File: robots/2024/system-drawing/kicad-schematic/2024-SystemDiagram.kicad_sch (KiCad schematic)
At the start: 184 parts

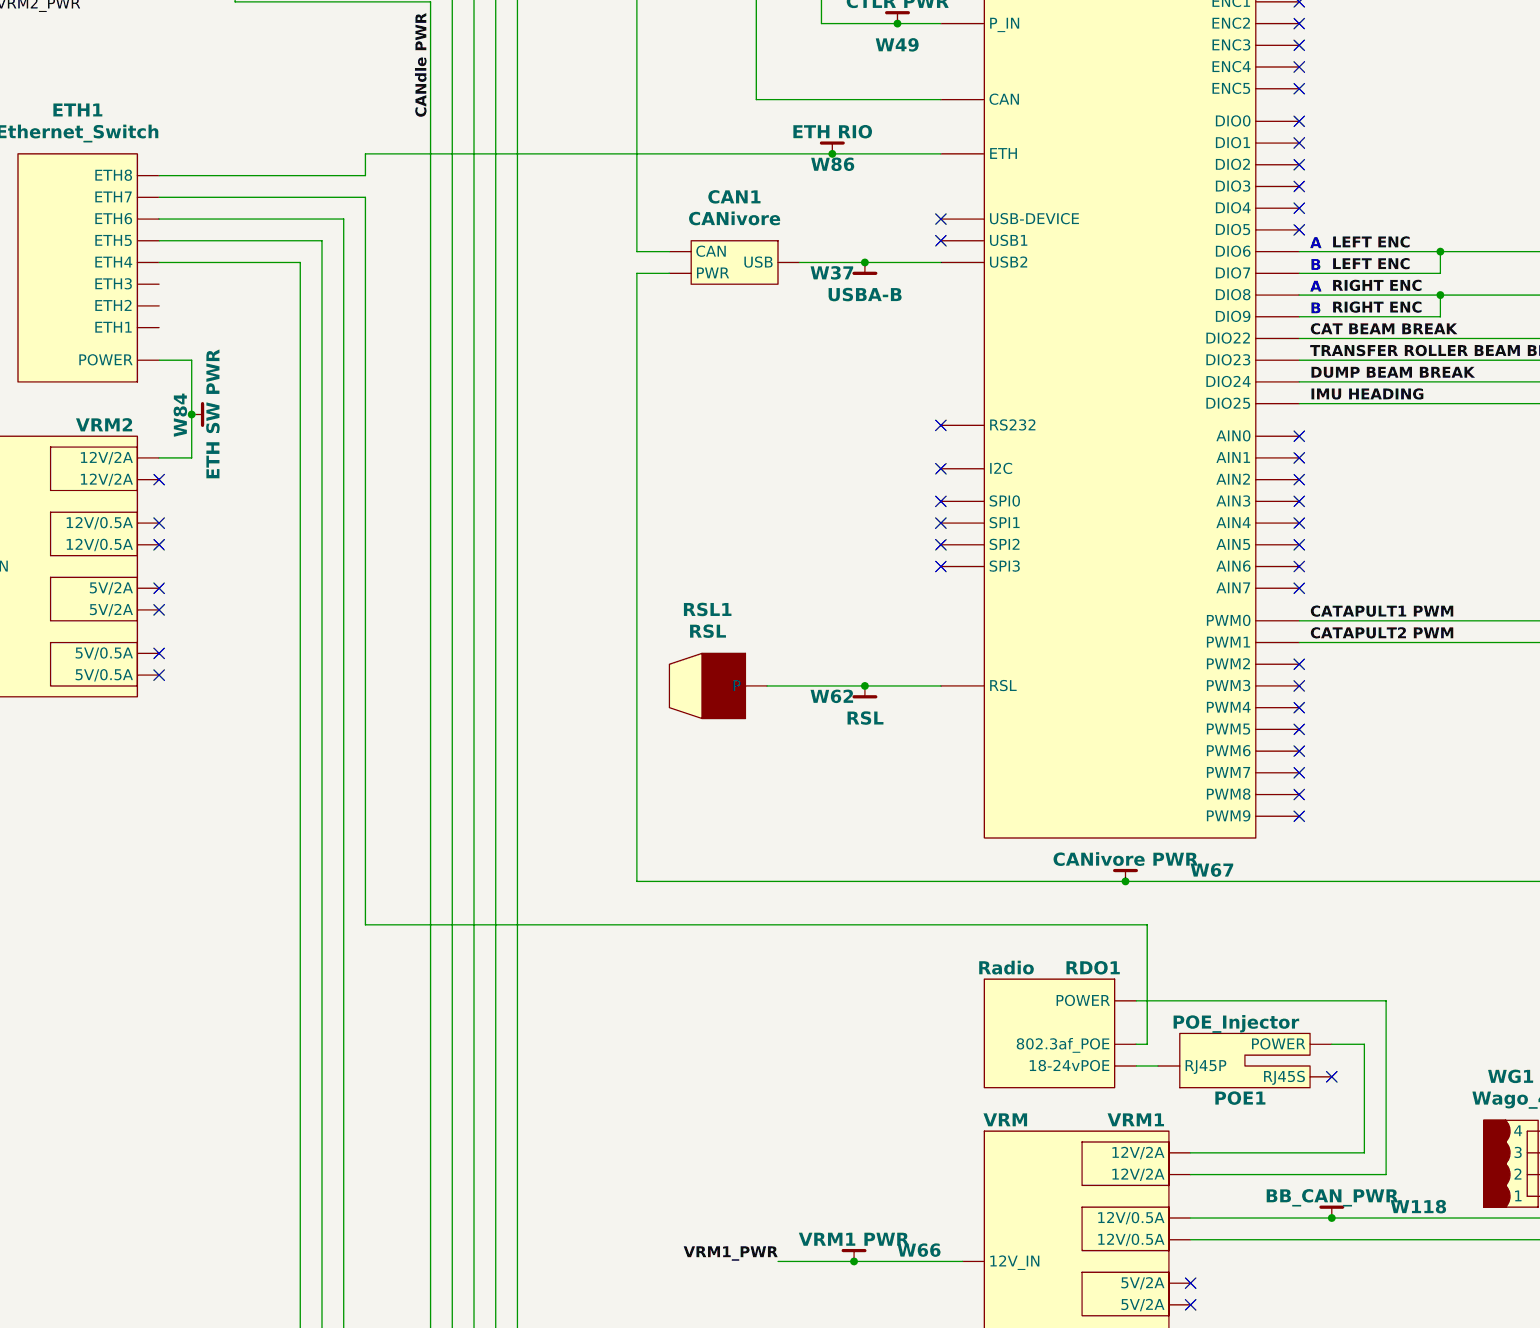
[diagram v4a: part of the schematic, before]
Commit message: Modified sys dwg rio ethernet, added comment to nx adapter
Signed-off-by: Scott Berman <sgberman1@gmail.com>
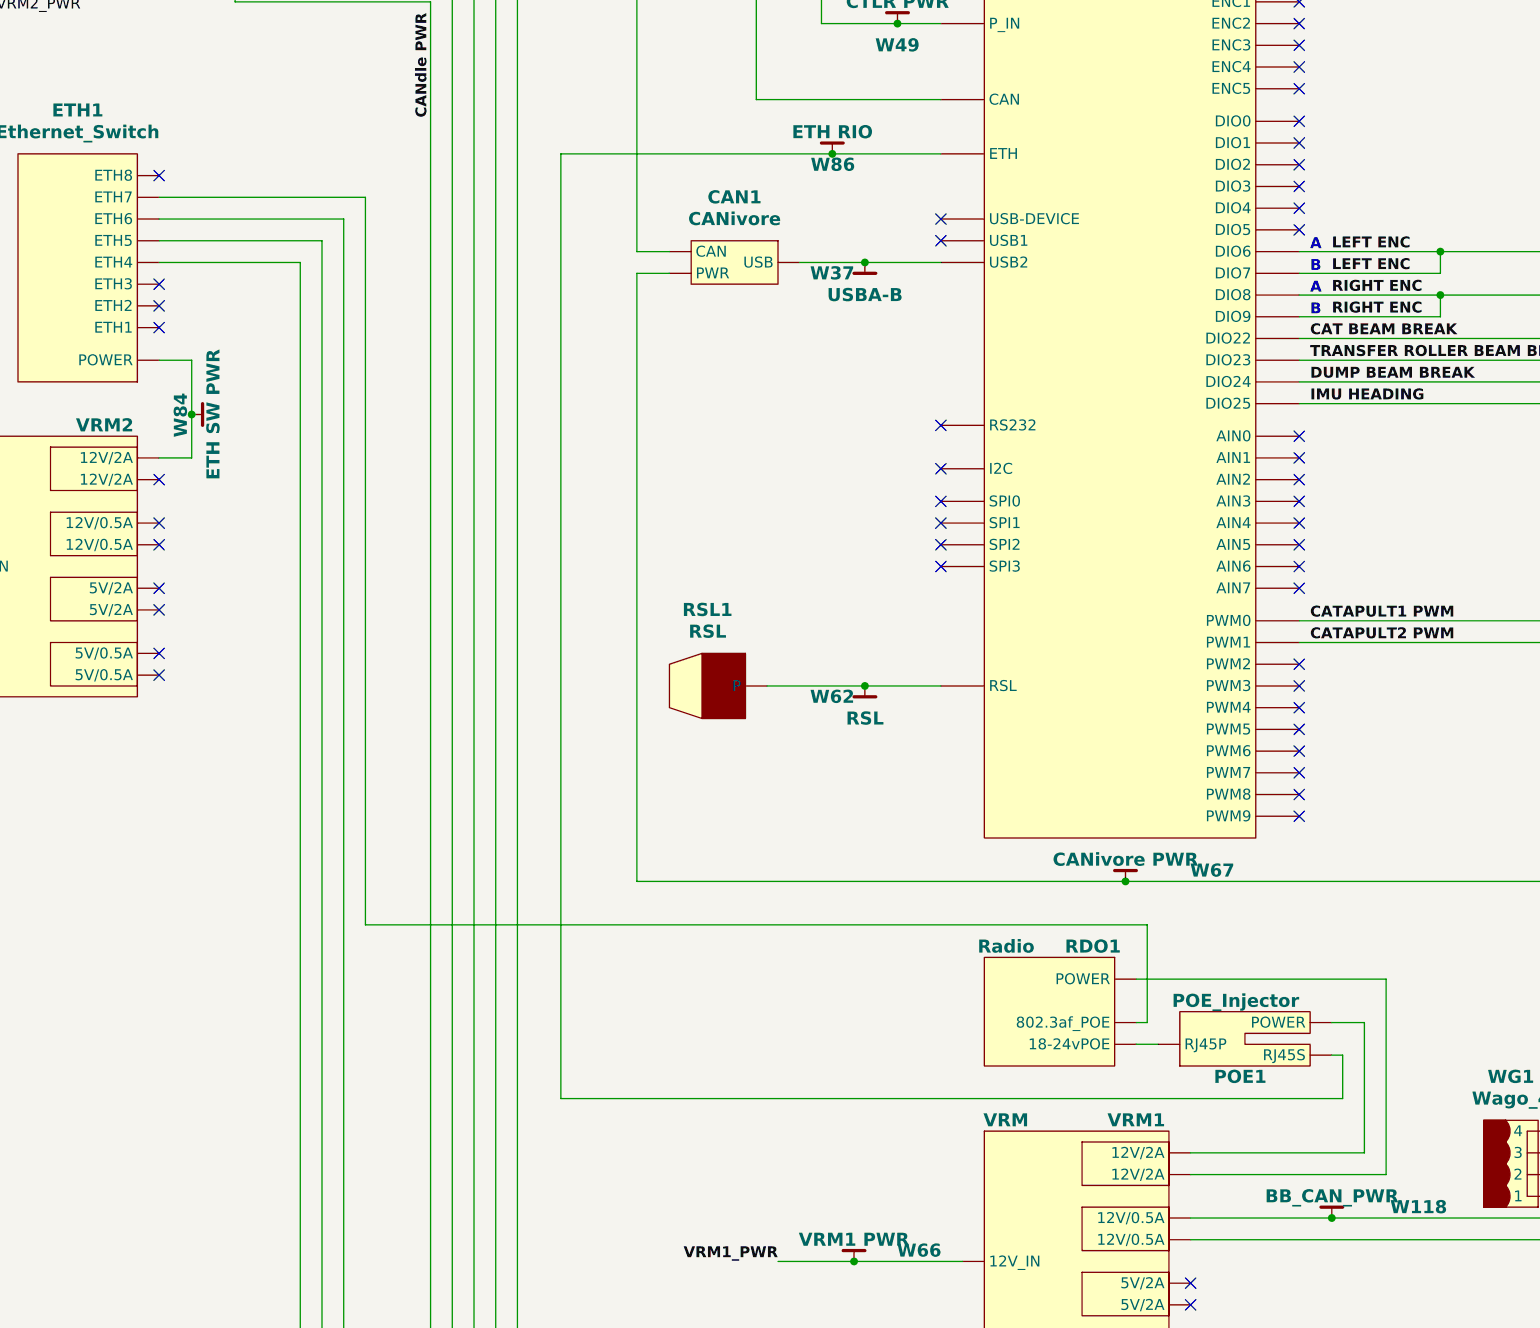
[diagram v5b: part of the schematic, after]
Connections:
- net at POE1. (RJ45S): now also RDO1. (POWER); no longer VRM1. (5V/2A)
- net at RDO1. (POWER): now also ETH1. (POWER); no longer VRM1. (5V/2A)
- net at RIO1.ETH, W86.: now also POE1. (RJ45S); no longer ETH1. (POWER)
- net at ETH1. (POWER): now also NX1. (Power), W87.; no longer RDO1. (POWER)
- new net: VRM1. (5V/2A), W118., WG1. (4)
- new net: POE1. (RJ45S), VRM1. (5V/2A)
- new net: RDO1. (POWER), VRM1. (5V/2A)
- new net: CAN1. (USB), W67., WG1. (4)
- new net: IND1. (P), MOT11. (PWR), W114.
- new net: MOT11. (PWR), MOT13. (PWR), W113.
- new net: ETH1. (POWER), NX2. (Power), W88.
- new net: MOT10. (PWR), MOT12. (PWR), W111.
- new net: MOT12. (PWR), MOT13. (PWR), W112.
- new net: VRM2. (5V/2A), W85., WG101. (3)
- new net: IND1. (P), MOT15. (PWR), W115.
- new net: ETH1. (POWER), VRM2. (5V/2A), W84.
- new net: ETH1. (POWER), NX3. (Power), W89.
- new net: PD2. (IN), WG101. (3)
- new net: MOT1. (PWR), MOT2. (PWR), W105.
- new net: MOT3. (PWR), MOT4. (PWR), W107.
- new net: IMU1. (RIO_PWM2), NX3. (Power), W47.
- now unconnected: VRM2. (5V/2A), VRM2. (5V/2A)
- no-connect marks 69 -> 72
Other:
- moved on the sheet: POE1, RDO1
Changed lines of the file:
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@@
   (no_connect (at 179.07 264.16))
   (no_connect (at 224.79 426.72))
+  (no_connect (at 87.63 236.22))
   (no_connect (at 87.63 264.16))
   (no_connect (at 220.98 259.08))
@@
   (no_connect (at 220.98 264.16))
   (no_connect (at 179.07 228.6))
+  (no_connect (at 87.63 223.52))
+  (no_connect (at 87.63 241.3))
+  (no_connect (at 87.63 238.76))
   (no_connect (at 191.77 434.34))
   (no_connect (at 224.79 398.78))
@@
   (no_connect (at 208.28 360.68))
   (no_connect (at 224.79 469.9))
-  (no_connect (at 224.79 328.93))
   (no_connect (at 179.07 266.7))
   (no_connect (at 220.98 298.45))
@@
     (stroke (width 0.254) (type default) (color 194 0 194 1))
   )
-  (wire (pts (xy 228.6 337.82) (xy 228.6 325.12))
+  (wire (pts (xy 228.6 337.82) (xy 228.6 322.58))
     (stroke (width 0.508) (type default) (color 255 0 0 1))
   )
@@
     (stroke (width 0.508) (type default) (color 255 0 0 1))
   )
-  (wire (pts (xy 231.14 340.36) (xy 231.14 320.04))
+  (wire (pts (xy 231.14 340.36) (xy 231.14 317.5))
     (stroke (width 0.508) (type default) (color 255 0 0 1))
   )
@@
   (wire (pts (xy 396.24 341.63) (xy 396.24 245.11))
     (stroke (width 0.254) (type default) (color 194 0 194 1))
+  )
+  (wire (pts (xy 134.62 331.47) (xy 226.06 331.47))
+    (stroke (width 0.508) (type default) (color 132 132 0 1))
   )
   (wire (pts (xy 586.74 132.08) (xy 605.79 132.08))
@@
     (stroke (width 0.254) (type default) (color 255 153 0 1))
   )
-  (wire (pts (xy 201.93 325.12) (xy 203.2 325.12))
-    (stroke (width 0.508) (type default) (color 132 132 0 1))
-  )
-  (wire (pts (xy 201.93 327.66) (xy 204.47 327.66))
+  (wire (pts (xy 201.93 322.58) (xy 203.2 322.58))
+    (stroke (width 0.508) (type default) (color 132 132 0 1))
+  )
+  (wire (pts (xy 201.93 325.12) (xy 204.47 325.12))
     (stroke (width 0.254) (type default) (color 255 0 0 1))
   )
@@
   (wire (pts (xy 487.68 72.39) (xy 552.45 72.39))
     (stroke (width 0.508) (type default) (color 255 0 0 1))
+  )
+  (wire (pts (xy 226.06 331.47) (xy 226.06 326.39))
+    (stroke (width 0.508) (type default) (color 132 132 0 1))
   )
   (wire (pts (xy 68.58 153.67) (xy 43.18 153.67))
@@
     (stroke (width 0) (type default))
   )
-  (wire (pts (xy 111.76 220.98) (xy 166.37 220.98))
+  (wire (pts (xy 134.62 220.98) (xy 166.37 220.98))
     (stroke (width 0.508) (type default) (color 132 132 0 1))
   )
@@
     (stroke (width 0.254) (type default) (color 255 153 0 1))
   )
-  (wire (pts (xy 203.2 325.12) (xy 203.2 311.15))
+  (wire (pts (xy 203.2 322.58) (xy 203.2 311.15))
     (stroke (width 0.508) (type default) (color 132 132 0 1))
   )
@@
     (stroke (width 0.254) (type default) (color 255 0 0 1))
   )
-  (wire (pts (xy 111.76 220.98) (xy 111.76 223.52))
-    (stroke (width 0.508) (type default) (color 132 132 0 1))
-  )
   (wire (pts (xy 586.74 328.93) (xy 607.06 328.93))
     (stroke (width 0.254) (type default) (color 255 153 0 1))
@@
     (stroke (width 0.254) (type default) (color 255 153 0 1))
   )
-  (wire (pts (xy 228.6 325.12) (xy 224.79 325.12))
+  (wire (pts (xy 228.6 322.58) (xy 224.79 322.58))
     (stroke (width 0.508) (type default) (color 255 0 0 1))
   )
@@
     (stroke (width 0.508) (type default) (color 255 0 0 1))
   )
+  (wire (pts (xy 134.62 220.98) (xy 134.62 331.47))
+    (stroke (width 0.508) (type default) (color 132 132 0 1))
+  )
   (wire (pts (xy 237.49 232.41) (xy 237.49 234.95))
     (stroke (width 0.254) (type default) (color 194 0 194 1))
@@
     (stroke (width 0.254) (type default) (color 255 153 0 1))
   )
-  (wire (pts (xy 201.93 320.04) (xy 231.14 320.04))
+  (wire (pts (xy 201.93 317.5) (xy 231.14 317.5))
     (stroke (width 0.508) (type default) (color 255 0 0 1))
   )
@@
     (stroke (width 0.254) (type default) (color 194 0 194 1))
   )
+  (wire (pts (xy 226.06 326.39) (xy 224.79 326.39))
+    (stroke (width 0.508) (type default) (color 132 132 0 1))
+  )
   (wire (pts (xy 121.92 494.03) (xy 121.92 185.42))
     (stroke (width 0.508) (type default) (color 255 0 0 1))
@@
   (wire (pts (xy 586.74 265.43) (xy 607.06 265.43))
     (stroke (width 0.254) (type default) (color 255 153 0 1))
-  )
-  (wire (pts (xy 111.76 223.52) (xy 87.63 223.52))
-    (stroke (width 0.508) (type default) (color 132 132 0 1))
   )
   (wire (pts (xy 579.12 210.82) (xy 574.04 210.82))
@@
     )
   )
-  (symbol (lib_id "SystemDiagram:POE_Injector") (at 222.25 330.2 180) (unit 1)
+  (symbol (lib_id "SystemDiagram:POE_Injector") (at 222.25 327.66 180) (unit 1)
     (in_bom yes) (on_board yes) (dnp no)
-    (property "Reference" "POE1" (at 217.17 331.47 0)
+    (property "Reference" "POE1" (at 217.17 328.93 0)
       (effects (font (face "FreeSans") (size 1.524 1.524) bold) (justify left))
     )
-    (property "Value" "POE_Injector" (at 220.98 322.58 0)
+    (property "Value" "POE_Injector" (at 220.98 320.04 0)
       (effects (font (face "FreeSans") (size 1.524 1.524) bold) (justify left))
     )
-    (property "Footprint" "" (at 222.25 330.2 0)
-      (effects (font (size 1.27 1.27)) hide)
-    )
-    (property "Datasheet" "" (at 222.25 330.2 0)
+    (property "Footprint" "" (at 222.25 327.66 0)
+      (effects (font (size 1.27 1.27)) hide)
+    )
+    (property "Datasheet" "" (at 222.25 327.66 0)
       (effects (font (size 1.27 1.27)) hide)
     )
@@
     )
   )
-  (symbol (lib_id "SystemDiagram:Radio") (at 199.39 317.5 0) (mirror y) (unit 1)
+  (symbol (lib_id "SystemDiagram:Radio") (at 199.39 314.96 0) (mirror y) (unit 1)
     (in_bom yes) (on_board yes) (dnp no)
-    (property "Reference" "RDO1" (at 196.85 316.23 0)
-      (effects (font (face "FreeSans") (size 1.524 1.524) bold))
-    )
-    (property "Value" "Radio" (at 186.69 316.23 0)
-      (effects (font (face "FreeSans") (size 1.524 1.524) bold))
-    )
-    (property "Footprint" "" (at 199.39 317.5 0)
-      (effects (font (size 1.27 1.27)) hide)
-    )
-    (property "Datasheet" "" (at 199.39 317.5 0)
-      (effects (font (size 1.27 1.27)) hide)
-    )
+    (property "Reference" "RDO1" (at 196.85 313.69 0)
+      (effects (font (face "FreeSans") (size 1.524 1.524) bold))
+    )
+    (property "Value" "Radio" (at 186.69 313.69 0)
+      (effects (font (face "FreeSans") (size 1.524 1.524) bold))
+    )
+    (property "Footprint" "" (at 199.39 314.96 0)
+      (effects (font (size 1.27 1.27)) hide)
+    )
+    (property "Datasheet" "" (at 199.39 314.96 0)
+      (effects (font (size 1.27 1.27)) hide)
+    )
